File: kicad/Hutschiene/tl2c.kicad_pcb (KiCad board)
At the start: 4 copper layers, 168.3 x 161.1 mm, 82 parts, among them IC101 ATTINY20-X, P101 12VDC, P102 RJ45, P103 CTL CONN, P104 TPI Header, P105 DRV CONN, P106 240VAC, P108 UG, P109 5VDC, P110 EG, P111 OG, P201 Mode_Bridge, P501 CONN_PIR_OG, P502 CONN_PIR_EG, P503 CONN_PIR_UG, Q301 IRLML2502, Q302 IRLML2502, Q303 IRLML2502, Q401 IRLML2502, Q402 IRLML2502, Q403 IRLML2502, SW101 TL3315NF160Q, U201 LF120ABDT-TR, U202 TPS70933

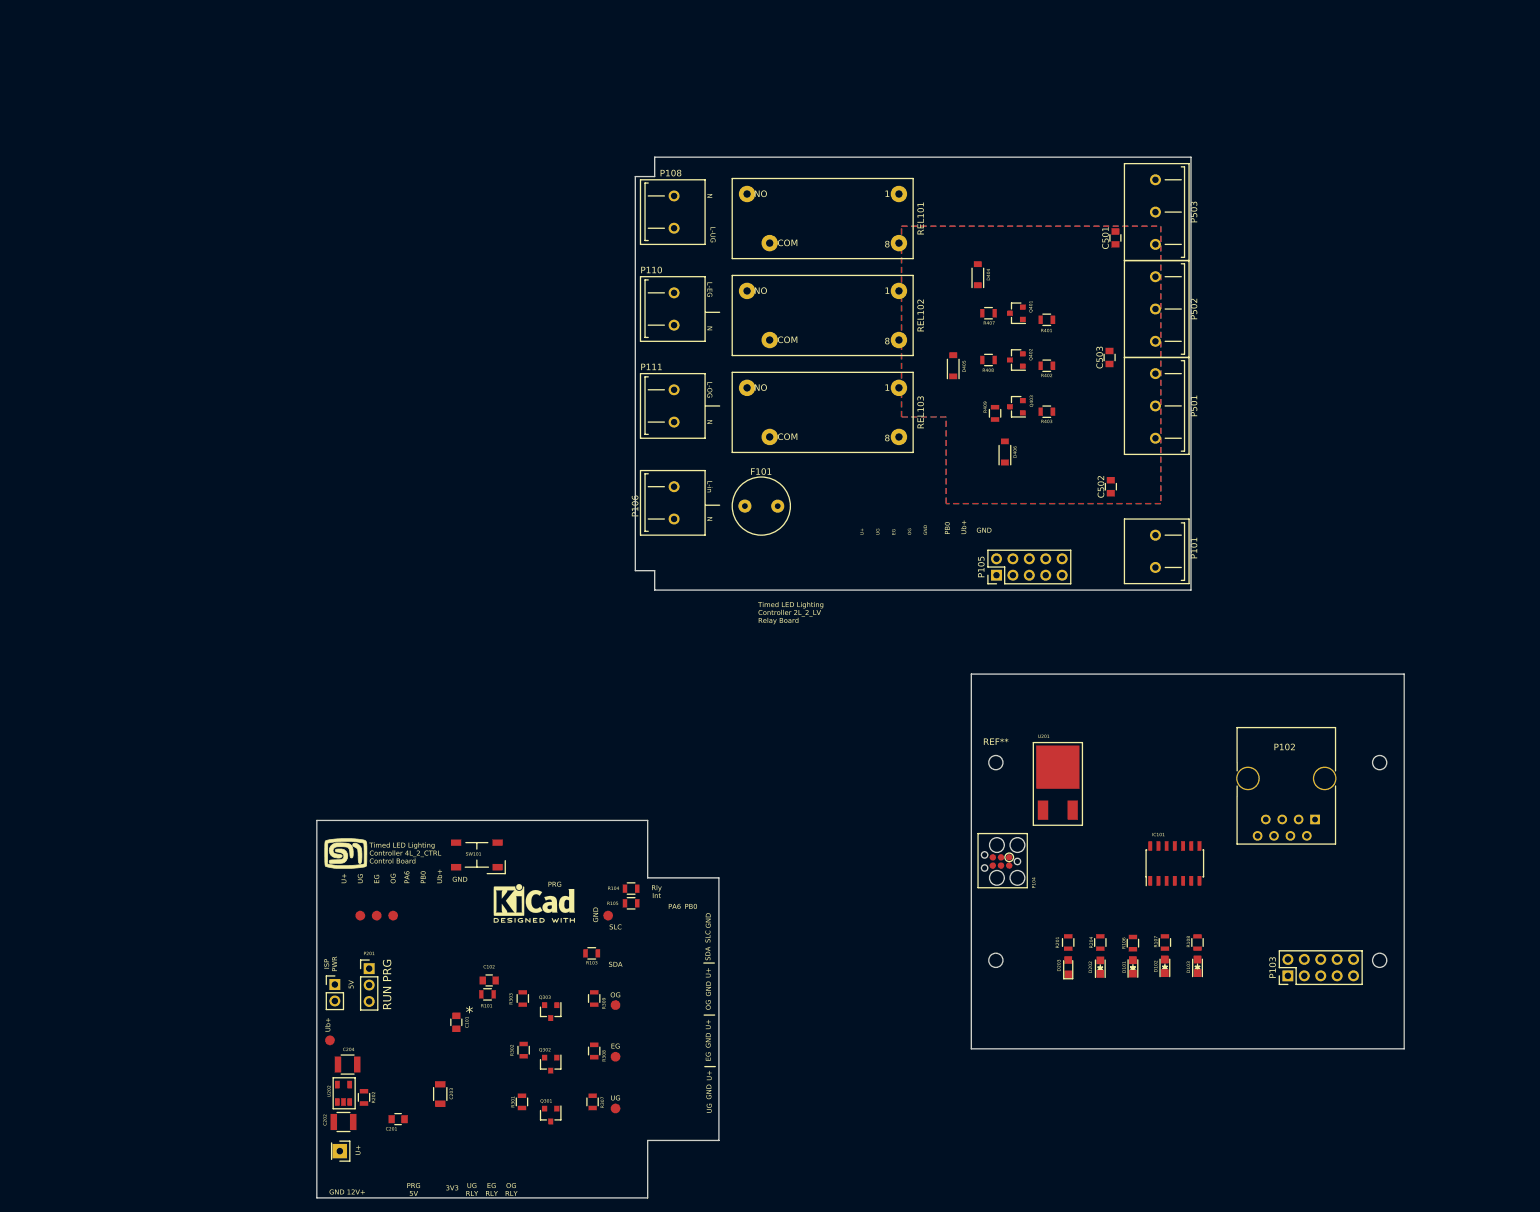
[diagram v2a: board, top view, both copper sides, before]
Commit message: Further work on the new Hutschiene Layout
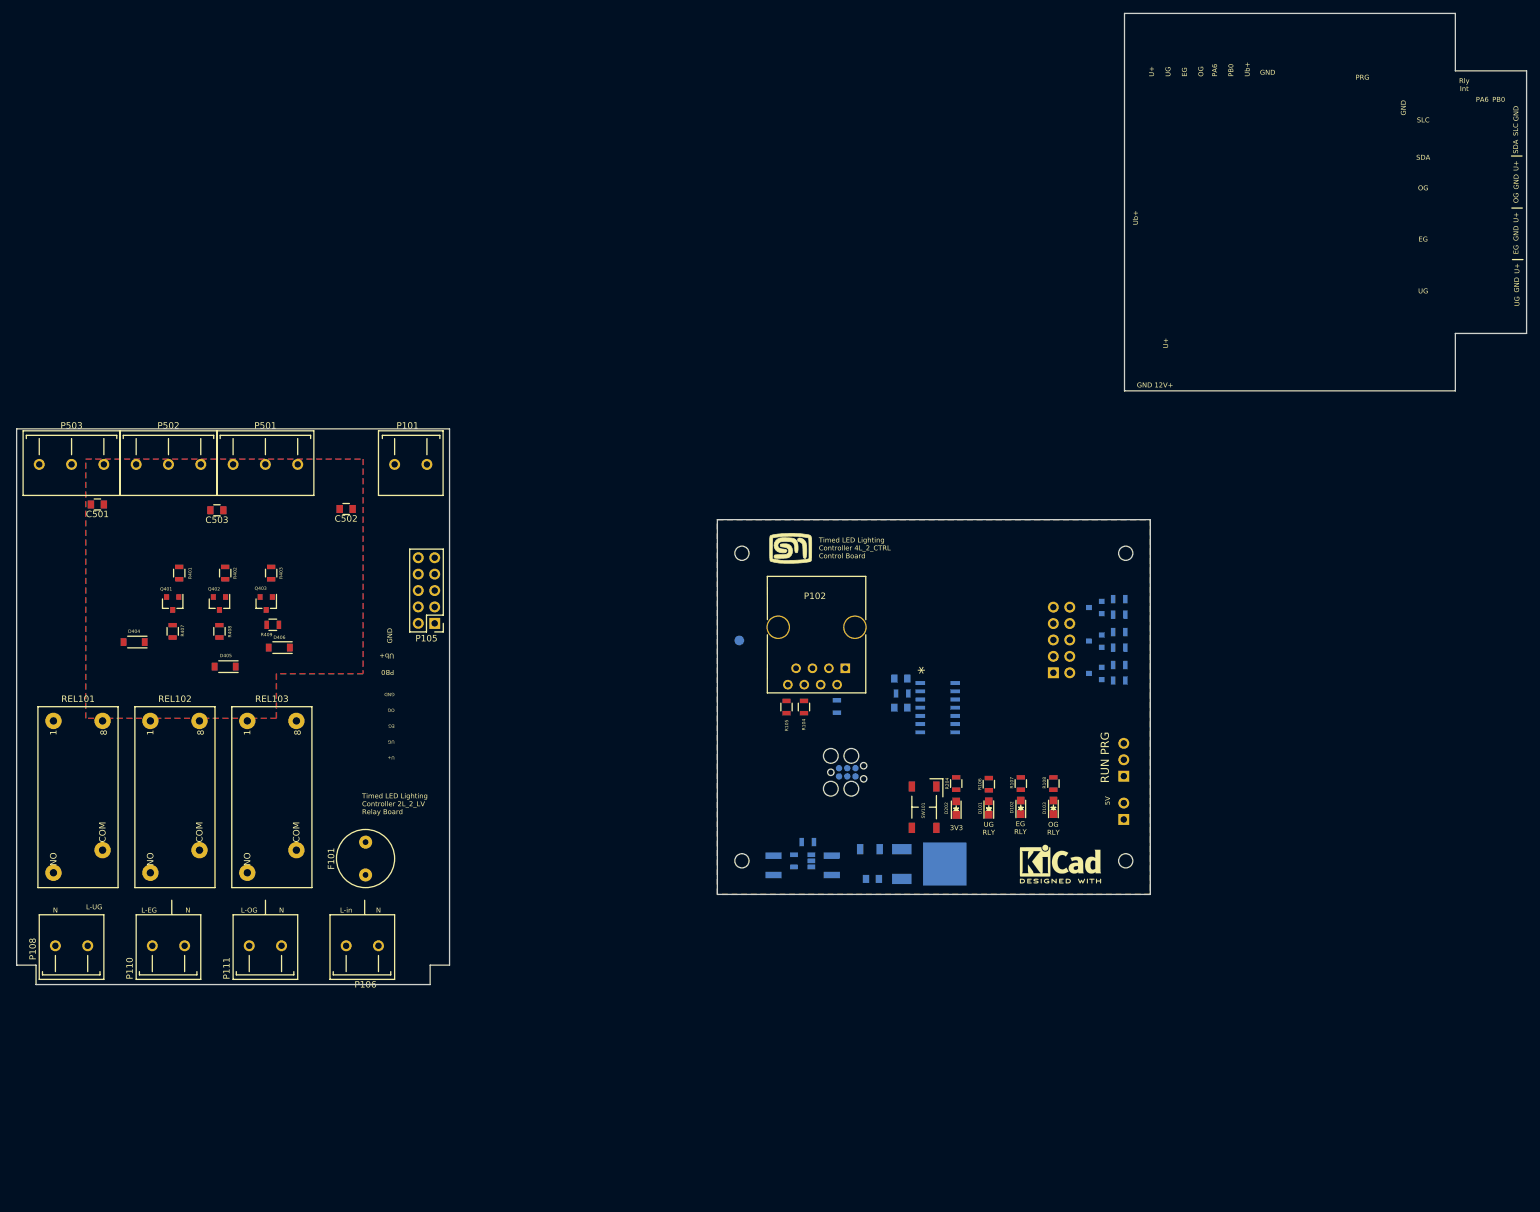
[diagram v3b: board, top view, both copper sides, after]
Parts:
- removed D203: 5VDC, LEDs:LED_0805
- removed R201: 660Ω, Resistors_SMD:R_0805
- removed TP104: TP_RLY_UG, Measurement_Points:Measurement_Point_Round-SMD-Pad_Small
- removed TP105: TP_RLY_EG, Measurement_Points:Measurement_Point_Round-SMD-Pad_Small
- removed TP106: TP_RLY_OG, Measurement_Points:Measurement_Point_Round-SMD-Pad_Small
- removed TP201: TP3V3, Measurement_Points:Measurement_Point_Round-SMD-Pad_Small
- removed TP202: TP12V, Pin_Headers:Pin_Header_Straight_1x01
- removed TP301: TP_UG, Measurement_Points:Measurement_Point_Round-SMD-Pad_Small
- removed TP302, TP303: TP_EG, Measurement_Points:Measurement_Point_Round-SMD-Pad_Small
- C101, C102, C201, C202, C203, C204, IC101, P103, P104, P109, P201, Q301, Q302, Q303, R101, R103, R202, R301, R302, R303, R307, R308, R309, TP101, U201, U202: moved to B.Cu
- moved P503 172.2 mm to (54.8, 65.5), turned to 180 degrees
- moved C501 162.9 mm to (58.8, 71.8), turned to 180 degrees
- moved P502 154.6 mm to (69.8, 65.5), turned to 180 degrees
- moved P108 150.5 mm to (52.2, 140.1), turned to 0 degrees
- moved REL101 146.0 mm to (55.8, 117.0), turned to 90 degrees
- moved D404 142.4 mm to (64.4, 93.0), turned to 180 degrees
- moved C503 140.2 mm to (77.2, 72.7), turned to 180 degrees
- moved R401 139.9 mm to (71.4, 82.4), turned to 90 degrees
- moved Q401 138.1 mm to (70.4, 87.1), turned to 270 degrees
- moved P501 138.0 mm to (84.8, 65.5), turned to 180 degrees
- moved R407 135.5 mm to (70.4, 91.4), turned to 90 degrees
- moved R402 131.1 mm to (78.5, 82.4), turned to 90 degrees
- moved P110 129.4 mm to (67.2, 140.1), turned to 0 degrees
- moved Q402 129.0 mm to (77.6, 87.1), turned to 270 degrees
- moved R408 126.2 mm to (77.6, 91.4), turned to 90 degrees
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- renumbered REF** to MNT1
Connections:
- P103 pad 1: /PIR13/U+ -> /RelayEG
- P103 pad 10: GND -> /PIR13/PIR_OG
- P103 pad 3: /RelayEG -> /PIR13/U+
- P103 pad 6: /GPIO_PB2 -> /PIR13/PIR_UG
- P103 pad 7: /PIR13/PIR_OG -> /GPIO_PB2
- P103 pad 9: /PIR13/PIR_UG -> GND
- P105 pad 1: /LED Driver/LED_DRIVER_U+ -> /LED Driver/Relay_EG
- P105 pad 10: GNDA -> /PIR_Connector/PIR_OG
- P105 pad 3: /LED Driver/Relay_EG -> /LED Driver/LED_DRIVER_U+
- P105 pad 6: (no net) -> /PIR_Connector/PIR_UG
- P105 pad 7: /PIR_Connector/PIR_OG -> (no net)
- P105 pad 9: /PIR_Connector/PIR_UG -> (no net)
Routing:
- added copper zone on U+, net /PIR13/U+
- added copper zone on Ub+, net /PIR13/Ub+
- added copper zone on B.Cu, net GND
- added copper zone on F.Cu, net GND
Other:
- board size 168.3 x 161.1 mm -> 233.7 x 150.3 mm
- board text removed: "PRG 5V"

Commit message: Further to the layout for the Hutschiene
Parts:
- removed G***: LOGO, tl2c-footprint:MyBasic_rounded_50_1
- removed REF***: KiCad-Logo2_6mm_SilkScreen, Symbols:KiCad-Logo2_6mm_SilkScreen
- C501, C502, C503, P105: moved to B.Cu
- moved R401 21.7 mm to (91.0, 91.8), turned to 0 degrees
- moved R402 18.4 mm to (90.8, 96.0), turned to 0 degrees
- moved R407 16.3 mm to (54.6, 95.2)
- moved Q401 16.2 mm to (54.6, 90.7)
- moved P105 14.8 mm to (98.3, 97.8), turned to 0 degrees
- moved D404 10.9 mm to (55.8, 99.5)
- moved C502 10.7 mm to (87.3, 68.4)
- moved R408 8.99 mm to (69.5, 95.2)
- moved Q402 8.93 mm to (69.5, 90.8)
- moved R403 8.00 mm to (90.8, 88.5), turned to 0 degrees
- moved D405 7.89 mm to (71.1, 99.5)
- moved C503 6.62 mm to (72.3, 68.2)
- moved D406 5.83 mm to (86.0, 99.7)
- moved R409 5.21 mm to (84.5, 95.4), turned to 90 degrees
- moved C501 4.01 mm to (57.1, 68.1)
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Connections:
- P101 pad 1: /Power System/U+In -> /DRV_PWR_IN
- P101 pad 2: GND -> GNDA
- P103 pad 5: /PIR13/Ub+ -> /Power System/U+In
- P105 pad 5: /PIR13/Ub+ -> /DRV_PWR_IN
- P105 pad 9: (no net) -> GNDA
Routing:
- net /Neutral: track 0.00 -> 62.2 mm
- net Net-(F101-Pad2): track 0.00 -> 41.2 mm
- net Net-(Q401-Pad1): track 0.00 -> 36.7 mm, vias 0 -> 2
- net /DRV_PWR_IN: track 0.00 -> 34.7 mm
- net /PIR_Connector/PIR_OG: track 0.00 -> 32.8 mm
- net Net-(Q402-Pad1): track 0.00 -> 22.7 mm, vias 0 -> 2
- net /LED Driver/LED_DRIVER_U+: track 0.00 -> 19.5 mm
- net /Lin: track 0.00 -> 12.2 mm
- net /LED Driver/Relay_OG: track 0.00 -> 11.8 mm
- net /LineUG: track 0.00 -> 11.4 mm
- net /LineOG: track 0.00 -> 11.4 mm
- net /LineEG: track 0.00 -> 11.4 mm
- net /LED Driver/Relay_UG: track 0.00 -> 11.4 mm
- net Net-(D404-Pad2): track 0.00 -> 10.2 mm
- net Net-(D405-Pad2): track 0.00 -> 10.2 mm
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
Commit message: Hutschiene layout intermediate save
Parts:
- moved P501 30.0 mm to (54.8, 65.5)
- moved P503 30.0 mm to (84.8, 65.5)
- moved C101 8.20 mm to (183.1, 106.9)
- moved R202 6.05 mm to (168.8, 130.1)
- moved R302 2.55 mm to (216.8, 94.0)
- moved R301 2.50 mm to (216.8, 99.1)
- moved R303 2.50 mm to (216.9, 88.9)
- moved R309 2.20 mm to (216.9, 86.6)
- moved R307 2.15 mm to (216.8, 96.8)
- moved R308 2.10 mm to (216.8, 91.8)
- moved R101 0.55 mm to (183.2, 101.5)
- moved C102 0.55 mm to (183.1, 103.8)
- moved R105 0.21 mm to (165.6, 103.0)
- moved R103 0.07 mm to (173.2, 103.0), turned to 270 degrees
- moved R104 0.07 mm to (168.2, 103.0)
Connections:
- P103 pad 4: /RelayOG -> /Power System/U+In
- P103 pad 5: /Power System/U+In -> /RelayOG
- P105 pad 4: /LED Driver/Relay_OG -> /DRV_PWR_IN
- P105 pad 5: /DRV_PWR_IN -> /LED Driver/Relay_OG
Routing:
- net Net-(C204-Pad1): track 0.00 -> 100.3 mm, vias 0 -> 1
- net /Power System/U+In: track 0.00 -> 58.8 mm, vias 0 -> 1
- net /GPIO_PB2: track 0.00 -> 56.9 mm
- net /PIR_Connector/PIR_EG: track 0.00 -> 52.9 mm
- net /PIR_Connector/PIR_UG: track 0.00 -> 43.5 mm
- net /~Reset: track 0.00 -> 34.9 mm, vias 0 -> 2
- net /PIR_Connector/PIR_OG: track 32.8 -> 62.4 mm
- net /PIR13/SIG_EG: track 0.00 -> 28.1 mm
- net /PIR13/SIG_UG: track 0.00 -> 26.6 mm
- net /RLY_INT: track 0.00 -> 25.2 mm
- net /TPIDATA: track 0.00 -> 22.8 mm
- net /SCL: track 0.00 -> 21.8 mm
- net /PIR13/U+: track 0.00 -> 18.6 mm, vias 0 -> 6
- net /TPICLK: track 0.00 -> 16.7 mm
- net /PIR13/Ub+: track 0.00 -> 12.7 mm, vias 0 -> 6
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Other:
- board size 233.7 x 150.3 mm -> 175.4 x 86 mm
- board text added: "+12V"
- board text added: "GND OG"
- board text added: "L EG"
- board text added: "L IN"
- board text added: "L OG"
- board text added: "L UG"
- board text added: "PIR EG"
- board text added: "PIR OG"
- board text added: "PIR UG"
- board text added: "V+ OG"
- board text removed: "EG"
- board text removed: "GND 12V+"
- board text removed: "L-EG"
- board text removed: "L-OG"
- board text removed: "L-UG"
- board text removed: "L-in"
- board text removed: "OG"
- board text removed: "PA6"
- board text removed: "PB0"
- board text removed: "PRG"
- board text removed: "Rly Int"
- board text removed: "SDA"
- board text removed: "SLC"
- board text removed: "U+"
- board text removed: "U+ UG EG OG GND"
- board text removed: "UG"
- board text removed: "Ub+"

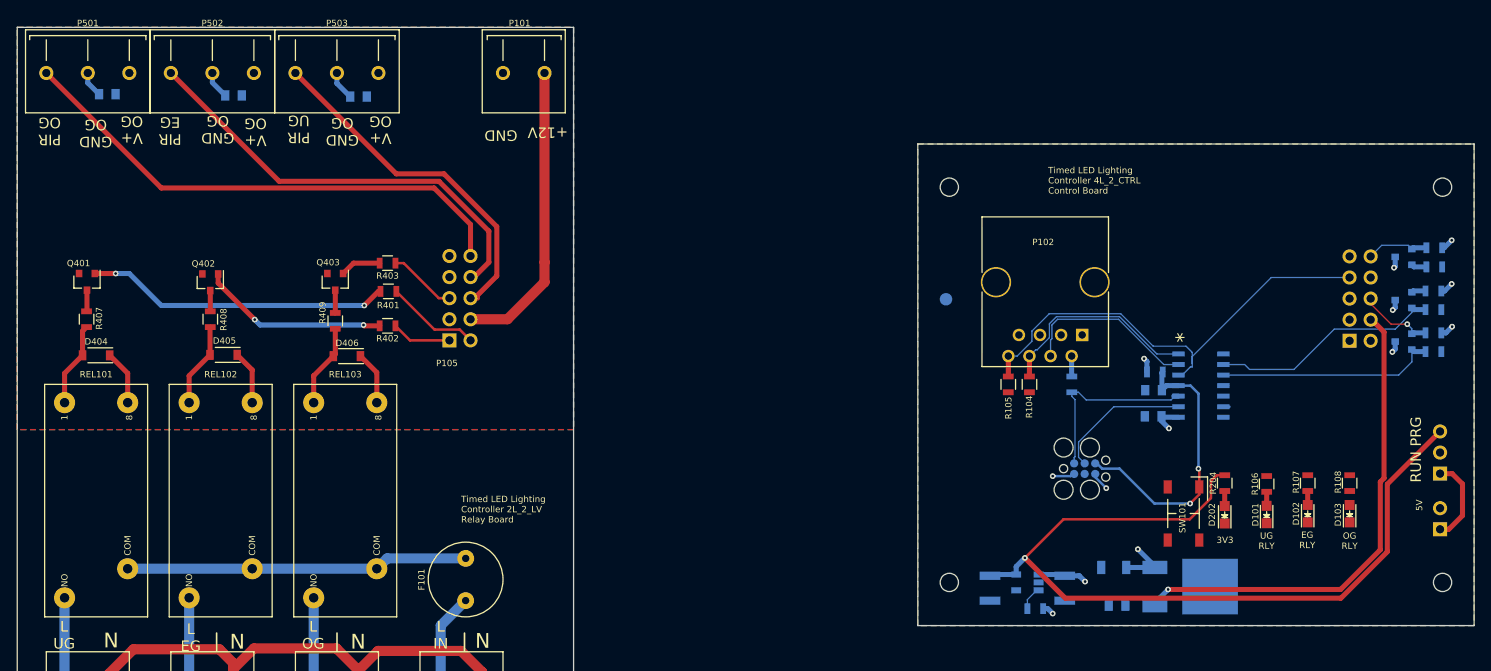
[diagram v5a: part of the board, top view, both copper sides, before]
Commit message: Completed draft of hutshiene layout
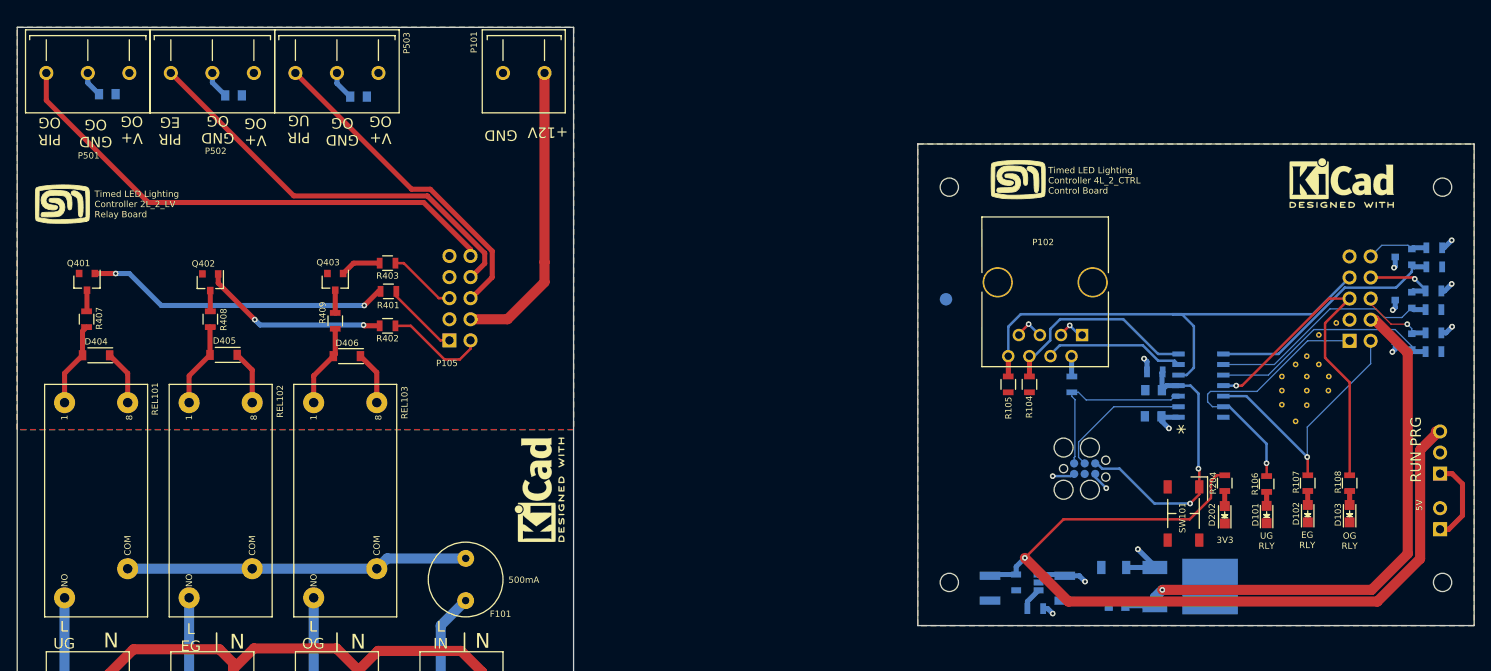
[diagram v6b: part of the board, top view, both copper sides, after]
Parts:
- added G***: LOGO, tl2c-footprint:MyBasic_rounded_50_1, F.Cu at (166.8, 78.3)
- added G***: LOGO, tl2c-footprint:MyBasic_rounded_50_1, F.Cu at (51.6, 81.3)
- added REF**: Stitch_VIA, tl2c-footprint:Stitch_VIA, F.Cu at (200.2, 100.7)
- added REF**: Stitch_VIA, tl2c-footprint:Stitch_VIA, F.Cu at (201.6, 99.7)
- added REF***: KiCad-Logo2_6mm_SilkScreen, Symbols:KiCad-Logo2_6mm_SilkScreen, F.Cu at (205.8, 78.8)
- added REF***: KiCad-Logo2_6mm_SilkScreen, Symbols:KiCad-Logo2_6mm_SilkScreen, F.Cu at (109.2, 115.8)
- added REF**11: Stitch_VIA, tl2c-footprint:Stitch_VIA, F.Cu at (198.6, 102.1)
- added REF**12: Stitch_VIA, tl2c-footprint:Stitch_VIA, F.Cu at (198.6, 103.8)
- added REF**13: Stitch_VIA, tl2c-footprint:Stitch_VIA, F.Cu at (200.2, 107.5)
- added REF**21: Stitch_VIA, tl2c-footprint:Stitch_VIA, F.Cu at (198.6, 105.5)
- added REF**22: Stitch_VIA, tl2c-footprint:Stitch_VIA, F.Cu at (201.6, 103.8)
- added REF**31: Stitch_VIA, tl2c-footprint:Stitch_VIA, F.Cu at (205.1, 95.7)
- added REF**31: Stitch_VIA, tl2c-footprint:Stitch_VIA, F.Cu at (203.0, 97.1)
- added REF**31: Stitch_VIA, tl2c-footprint:Stitch_VIA, F.Cu at (203.0, 100.7)
- added REF**31: Stitch_VIA, tl2c-footprint:Stitch_VIA, F.Cu at (201.6, 102.1)
- added REF**32: Stitch_VIA, tl2c-footprint:Stitch_VIA, F.Cu at (204.2, 102.1)
- added REF**41: Stitch_VIA, tl2c-footprint:Stitch_VIA, F.Cu at (204.2, 103.8)
- added REF**42: Stitch_VIA, tl2c-footprint:Stitch_VIA, F.Cu at (201.6, 105.5)
- P102: footprint Connect:RJ45_8 -> tl2c-footprint:RJ45_8P8C
- moved P102 9.26 mm to (165.6, 99.7)
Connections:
- P103 pad 1: /RelayEG -> /RelayUG
- P103 pad 2: /RelayUG -> /RelayEG
- P105 pad 1: /LED Driver/Relay_EG -> /LED Driver/Relay_UG
- P105 pad 2: /LED Driver/Relay_UG -> /LED Driver/Relay_EG
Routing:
- net /RelayOG: track 0.78 -> 44.0 mm, vias 0 -> 1
- net /RelayUG: track 0.74 -> 33.8 mm, vias 0 -> 1
- net /RelayEG: track 0.42 -> 32.9 mm, vias 0 -> 1
- net /PIR13/SIG_OG: track 1.85 -> 29.5 mm
- net /Power System/U+In: track 58.8 -> 68.0 mm
- net /PIR13/PIR_EG: track 1.71 -> 9.08 mm, vias 0 -> 1
- net GND: track 2.27 -> 9.52 mm, vias 1 -> 3
- net /LED Driver/Relay_EG: track 7.22 -> 12.3 mm
- net /SCL: track 21.8 -> 17.0 mm
- net Net-(C204-Pad1): track 100.3 -> 104.1 mm
- net /PIR_Connector/PIR_UG: track 43.5 -> 39.9 mm
- net /GPIO_PB2: track 56.9 -> 60.4 mm
- net /LED Driver/Relay_UG: track 11.4 -> 9.20 mm
- net /PIR_Connector/PIR_EG: track 52.9 -> 51.0 mm
- net Net-(D103-Pad2): track 0.00 -> 1.68 mm
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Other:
- board text added: "500mA"

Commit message: Reworked the layout for the CamdenBoss enclosure
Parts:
- removed MNT1 (x4): MountingHole_2.2mm_M2, Mounting_Holes:MountingHole_2.2mm_M2
- removed REF*** (x2): KiCad-Logo2_6mm_SilkScreen, Symbols:KiCad-Logo2_6mm_SilkScreen
- added G***: LOGO, tl2c-footprint:KiCad_LOGO_9mm, F.Cu at (200.9, 79.8)
- added G***: LOGO, tl2c-footprint:KiCad_LOGO_9mm, F.Cu at (108.1, 103.5)
- added G***: LOGO, tl2c-footprint:MyBasic_rounded_50_1, B.Cu at (211.0, 78.4)
- added G***: LOGO, tl2c-footprint:KiCad_LOGO_9mm, B.Cu at (167.1, 79.9)
- moved G*** 48.8 mm to (166.9, 127.2)
- moved R202 0.45 mm to (168.8, 129.6)
- moved U201 0.45 mm to (189.9, 127.0)
- moved U202 0.45 mm to (167.9, 126.5)
- moved C201 0.45 mm to (178.7, 129.2)
- moved C202 0.45 mm to (172.4, 127.2)
- moved C203 0.45 mm to (178.3, 124.7)
- moved C204 0.45 mm to (163.4, 127.2)
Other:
- board size 175.4 x 86 mm -> 175.9 x 86.5 mm
